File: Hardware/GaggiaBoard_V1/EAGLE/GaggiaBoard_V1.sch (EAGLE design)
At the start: 112 parts, among them IC1 LD117ADT33TR, J10 PIN262409-1, J11 PIN262409-1, J12 PIN262409-1, J13 PIN262409-1, J14 PIN262409-1, J15 PIN262409-1, J16 PIN262409-1, J17 PIN262409-1, J18 PIN262409-1, J19 PIN262409-1, J2 QWIIC_RIGHT_ANGLE, J20 PIN262409-1, J21 PIN262409-1, J22 PIN262409-1, J23 PIN262409-1, J24 5033981892, J3 QWIIC_RIGHT_ANGLE, J4 1X2-3.5MM, J5 1X2-3.5MM, K1 RELAY-SPDT-JZC-11F, K2 RELAY-SPDT-JZC-11F, K3 RELAY-SPDT-JZC-11F, Q1 600mA/40V, Q2 600mA/40V, Q3 600mA/40V, Q4 600mA/40V, Q5 600mA/40V, Q6 600mA/40V, Q8 600mA/40V, Q9 600mA/40V, U1 BLACKPILL, U2 MAX31855K, U3 MAX31855K, U5 TXS0102, U6 TXU0102

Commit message: Layout update
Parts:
- added C12: 1nF/250V, rcl:C-USC0603
- added C13: 10uF/16V, rcl:C-USC0603
- added D5: 1N4007, diode:DIODE-DO214AC
- added IC2: LD117AS33TR, v-reg:LD117AS33TR
- added Q10: 600mA/40V, SparkFun-DiscreteSemi:TRANS_NPN-MMBT2222AL
- added R27, R28: 10K, rcl:R-US_R0603
- IC1: value LD117ADT33TR -> LD117AS33TR; device v-reg:LD117ADT33TR -> v-reg:LD117AS33TR
- J1: LCSC C163037 -> C144395
- J2, J3: value QWIIC_RIGHT_ANGLE -> Vertical Qwiic Connector; device SparkFun-Connectors:QWIIC_CONNECTORJS-1MM -> SparkFun-Connectors:QWIIC_CONNECTOR; LCSC C160404 -> C160390
- J6, J7, J9: device SparkFun-Connectors:CONN_03JST-PTH -> SparkFun-Connectors:CONN_03JST-PTH-VERT; LCSC C157929 -> C131339
- J8: device SparkFun-Connectors:CONN_05JST -> SparkFun-Connectors:CONN_05JST-VERT; LCSC C157923 -> C157993
- R1: value 220K -> 470; device rcl:R-US_R1206 -> rcl:R-US_R0603; LCSC C130275 -> C114669
- R12: value 120 -> 51; LCSC C114640 -> C114628
- R13: value 10K -> 220; device rcl:R-US_R0603 -> rcl:R-US_R2512; LCSC C98220 -> C877859
- R14: value 51 -> 10K; LCSC C114628 -> C98220
- R15: value 220 -> 1K; device rcl:R-US_R2512 -> rcl:R-US_R0603; LCSC C877859 -> C22548
- R20, R21: value 10K -> 220K; device rcl:R-US_R0603 -> rcl:R-US_R1206; LCSC C98220 -> C130275
- R22: value 100 -> 22K; LCSC C105588 -> C114065
- R9: value 470 -> 120; LCSC C114669 -> C114640
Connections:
- new net N$43: C6.2, D5.A, Q10.E
- new net N$44: OK1.A, R15.2
- new net N$45: B1.+, C6.1, R15.1, R22.2
- net 3V3: now also C13.1, IC2.OUT, R14.2, R27.2; no longer R13.2, R21.2
- net 5V: now also IC2.IN, R9.2; no longer R12.2
- net AC_N: now also R21.1; no longer B1.AC2
- net AC_P: now also R20.1; no longer R1.1
- net GND: now also C13.2, IC2.ADJ, R12.1; no longer C6.2, R14.1
- net N$2: now also B1.-, D5.C, Q10.B, R22.1; no longer B1.+, OK1.A
- net N$24: now also R9.1; no longer R10.1
- net N$27: now also R12.2; no longer R14.2
- net N$28: now also R10.1; no longer R11.1
- net N$29: now also R11.1; no longer R12.1
- net N$32: now also R13.2; no longer R15.2
- net N$34: now also R28.2; no longer R20.2
- net N$35: now also R27.1; no longer R21.1
- net N$36: now also B1.AC1, C12.2, R21.2; no longer OK1.COL, R13.1, R22.1
- net N$37: now also B1.AC2, C12.1, R20.2; no longer B1.AC1, R1.2
- net N$39: now also R1.2; no longer R9.2
- net N$7: now also Q10.C; no longer B1.-
- net PA0: now also OK1.COL, R14.1; no longer C6.1, R22.2
- net PB5: now also R28.1; no longer R20.1
- net PB8: now also R1.1; no longer R9.1
- net PUMP_N: now also R13.1; no longer R15.1
- net UART6_5V_RX: now also J1.2; no longer J1.3
- net UART6_5V_TX: now also J1.3; no longer J1.2
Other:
- moved on the sheet: B1, C2, C6, C7, C8, C9, F1, IC1, J22, J23, J9, LED4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

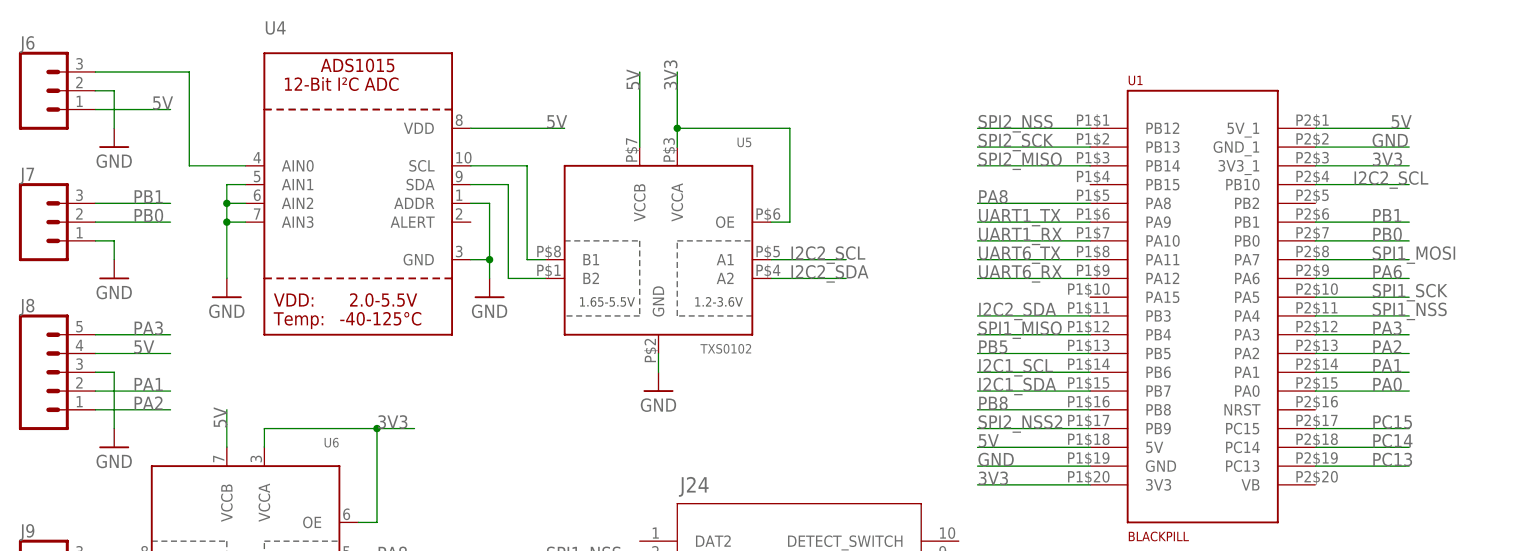
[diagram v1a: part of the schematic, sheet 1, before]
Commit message: Scales port change to PB
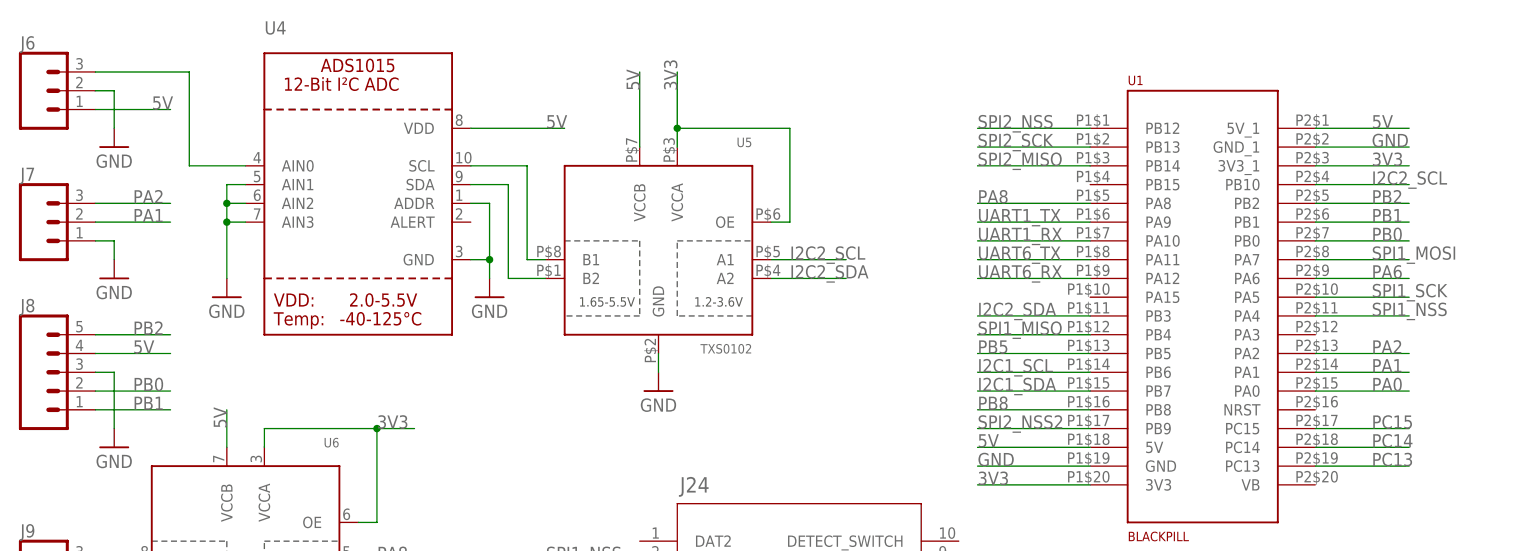
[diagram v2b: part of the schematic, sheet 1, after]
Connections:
- removed net PA3: J8.5, U1.PA3
- new net PB2: J8.5, U1.PB2
- net PA1: now also J7.2; no longer J8.2
- net PA2: now also J7.3; no longer J8.1
- net PB0: now also J8.2; no longer J7.2
- net PB1: now also J8.1; no longer J7.3
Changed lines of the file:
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@@
 <pinref part="U1" gate="G$1" pin="5V_1"/>
 <wire x1="218.44" y1="167.64" x2="231.14" y2="167.64" width="0.1524" layer="91"/>
-<label x="228.6" y="167.64" size="1.778" layer="95"/>
+<label x="226.06" y="167.64" size="1.778" layer="95"/>
 </segment>
 <segment>
@@
 <pinref part="U1" gate="G$1" pin="PB10"/>
 <wire x1="218.44" y1="160.02" x2="231.14" y2="160.02" width="0.1524" layer="91"/>
-<label x="223.52" y="160.02" size="1.778" layer="95"/>
+<label x="226.06" y="160.02" size="1.778" layer="95"/>
 </segment>
 <segment>
@@
 </segment>
 <segment>
-<label x="58.42" y="132.08" size="1.778" layer="95"/>
-<pinref part="J8" gate="G$1" pin="2"/>
-<wire x1="53.34" y1="132.08" x2="63.5" y2="132.08" width="0.1524" layer="91"/>
+<pinref part="J7" gate="J$1" pin="2"/>
+<wire x1="53.34" y1="154.94" x2="63.5" y2="154.94" width="0.1524" layer="91"/>
+<label x="58.42" y="154.94" size="1.778" layer="95"/>
 </segment>
 </net>
@@
 </segment>
 </net>
-<net name="PA3" class="0">
-<segment>
-<pinref part="U1" gate="G$1" pin="PA3"/>
-<wire x1="218.44" y1="139.7" x2="231.14" y2="139.7" width="0.1524" layer="91"/>
-<label x="226.06" y="139.7" size="1.778" layer="95"/>
-</segment>
-<segment>
-<pinref part="J8" gate="G$1" pin="5"/>
-<wire x1="53.34" y1="139.7" x2="63.5" y2="139.7" width="0.1524" layer="91"/>
-<label x="58.42" y="139.7" size="1.778" layer="95"/>
-</segment>
-</net>
 <net name="PA2" class="0">
 <segment>
@@
 </segment>
 <segment>
+<pinref part="J7" gate="J$1" pin="3"/>
+<wire x1="53.34" y1="157.48" x2="63.5" y2="157.48" width="0.1524" layer="91"/>
+<label x="58.42" y="157.48" size="1.778" layer="95"/>
+</segment>
+</net>
+<net name="PB8" class="0">
+<segment>
+<pinref part="U1" gate="G$1" pin="PB8"/>
+<wire x1="187.96" y1="129.54" x2="172.72" y2="129.54" width="0.1524" layer="91"/>
+<label x="172.72" y="129.54" size="1.778" layer="95"/>
+</segment>
+</net>
+<net name="PC15" class="0">
+<segment>
+<pinref part="U1" gate="G$1" pin="PC15"/>
+<wire x1="218.44" y1="127" x2="231.14" y2="127" width="0.1524" layer="91"/>
+<label x="226.06" y="127" size="1.778" layer="95"/>
+</segment>
+</net>
+<net name="PC14" class="0">
+<segment>
+<pinref part="U1" gate="G$1" pin="PC14"/>
+<wire x1="218.44" y1="124.46" x2="231.14" y2="124.46" width="0.1524" layer="91"/>
+<label x="226.06" y="124.46" size="1.778" layer="95"/>
+</segment>
+</net>
+<net name="PC13" class="0">
+<segment>
+<pinref part="U1" gate="G$1" pin="PC13"/>
+<wire x1="218.44" y1="121.92" x2="231.14" y2="121.92" width="0.1524" layer="91"/>
+<label x="226.06" y="121.92" size="1.778" layer="95"/>
+</segment>
+</net>
+<net name="PB0" class="0">
+<segment>
+<pinref part="U1" gate="G$1" pin="PB0"/>
+<wire x1="218.44" y1="152.4" x2="231.14" y2="152.4" width="0.1524" layer="91"/>
+<label x="226.06" y="152.4" size="1.778" layer="95"/>
+</segment>
+<segment>
+<pinref part="J8" gate="G$1" pin="2"/>
+<wire x1="53.34" y1="132.08" x2="63.5" y2="132.08" width="0.1524" layer="91"/>
+<label x="58.42" y="132.08" size="1.778" layer="95"/>
+</segment>
+</net>
+<net name="PB1" class="0">
+<segment>
+<pinref part="U1" gate="G$1" pin="PB1"/>
+<wire x1="218.44" y1="154.94" x2="231.14" y2="154.94" width="0.1524" layer="91"/>
+<label x="226.06" y="154.94" size="1.778" layer="95"/>
+</segment>
+<segment>
 <pinref part="J8" gate="G$1" pin="1"/>
 <wire x1="53.34" y1="129.54" x2="63.5" y2="129.54" width="0.1524" layer="91"/>
 <label x="58.42" y="129.54" size="1.778" layer="95"/>
-</segment>
-</net>
-<net name="PB8" class="0">
-<segment>
-<pinref part="U1" gate="G$1" pin="PB8"/>
-<wire x1="187.96" y1="129.54" x2="172.72" y2="129.54" width="0.1524" layer="91"/>
-<label x="172.72" y="129.54" size="1.778" layer="95"/>
-</segment>
-</net>
-<net name="PC15" class="0">
-<segment>
-<pinref part="U1" gate="G$1" pin="PC15"/>
-<wire x1="218.44" y1="127" x2="231.14" y2="127" width="0.1524" layer="91"/>
-<label x="226.06" y="127" size="1.778" layer="95"/>
-</segment>
-</net>
-<net name="PC14" class="0">
-<segment>
-<pinref part="U1" gate="G$1" pin="PC14"/>
-<wire x1="218.44" y1="124.46" x2="231.14" y2="124.46" width="0.1524" layer="91"/>
-<label x="226.06" y="124.46" size="1.778" layer="95"/>
-</segment>
-</net>
-<net name="PC13" class="0">
-<segment>
-<pinref part="U1" gate="G$1" pin="PC13"/>
-<wire x1="218.44" y1="121.92" x2="231.14" y2="121.92" width="0.1524" layer="91"/>
-<label x="226.06" y="121.92" size="1.778" layer="95"/>
-</segment>
-</net>
-<net name="PB0" class="0">
-<segment>
-<pinref part="U1" gate="G$1" pin="PB0"/>
-<wire x1="218.44" y1="152.4" x2="231.14" y2="152.4" width="0.1524" layer="91"/>
-<label x="226.06" y="152.4" size="1.778" layer="95"/>
-</segment>
-<segment>
-<pinref part="J7" gate="J$1" pin="2"/>
-<wire x1="53.34" y1="154.94" x2="63.5" y2="154.94" width="0.1524" layer="91"/>
-<label x="58.42" y="154.94" size="1.778" layer="95"/>
-</segment>
-</net>
-<net name="PB1" class="0">
-<segment>
-<pinref part="U1" gate="G$1" pin="PB1"/>
-<wire x1="218.44" y1="154.94" x2="231.14" y2="154.94" width="0.1524" layer="91"/>
-<label x="226.06" y="154.94" size="1.778" layer="95"/>
-</segment>
-<segment>
-<pinref part="J7" gate="J$1" pin="3"/>
-<wire x1="53.34" y1="157.48" x2="63.5" y2="157.48" width="0.1524" layer="91"/>
-<label x="58.42" y="157.48" size="1.778" layer="95"/>
 </segment>
 </net>
@@
 </segment>
 </net>
+<net name="PB2" class="0">
+<segment>
+<pinref part="U1" gate="G$1" pin="PB2"/>
+<wire x1="218.44" y1="157.48" x2="231.14" y2="157.48" width="0.1524" layer="91"/>
+<label x="226.06" y="157.48" size="1.778" layer="95"/>
+</segment>
+<segment>
+<pinref part="J8" gate="G$1" pin="5"/>
+<wire x1="53.34" y1="139.7" x2="63.5" y2="139.7" width="0.1524" layer="91"/>
+<label x="58.42" y="139.7" size="1.778" layer="95"/>
+</segment>
+</net>

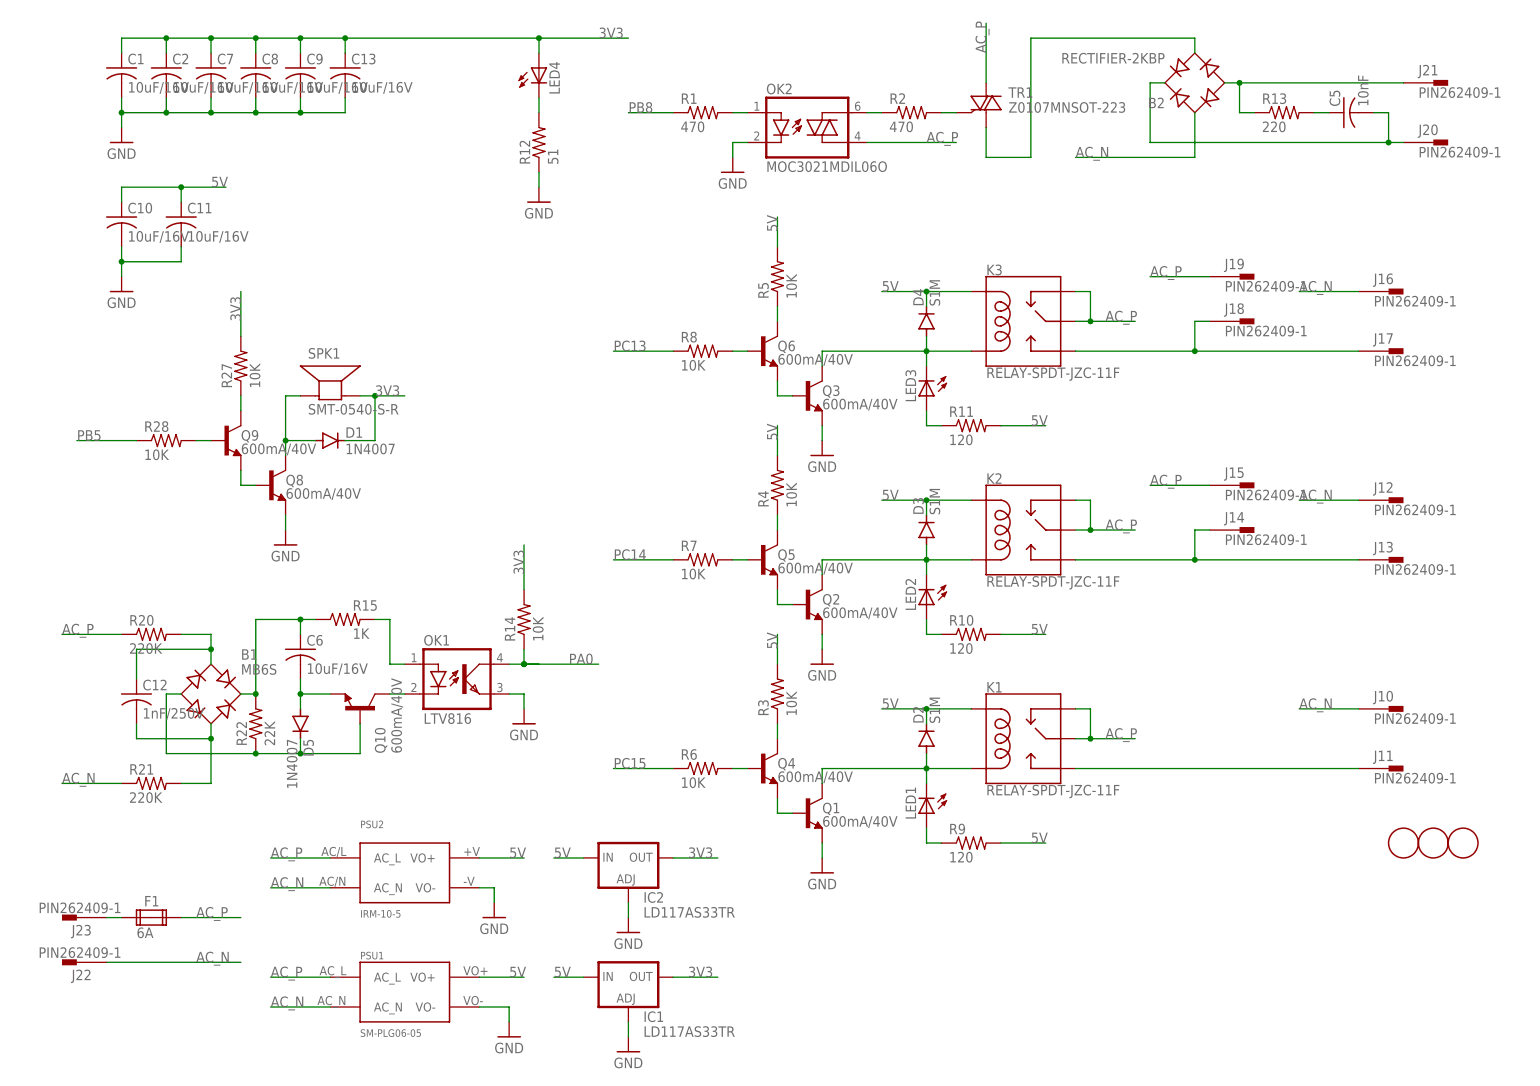
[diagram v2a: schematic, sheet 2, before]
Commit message: Pump bridge rectifier removed, SSR control changed
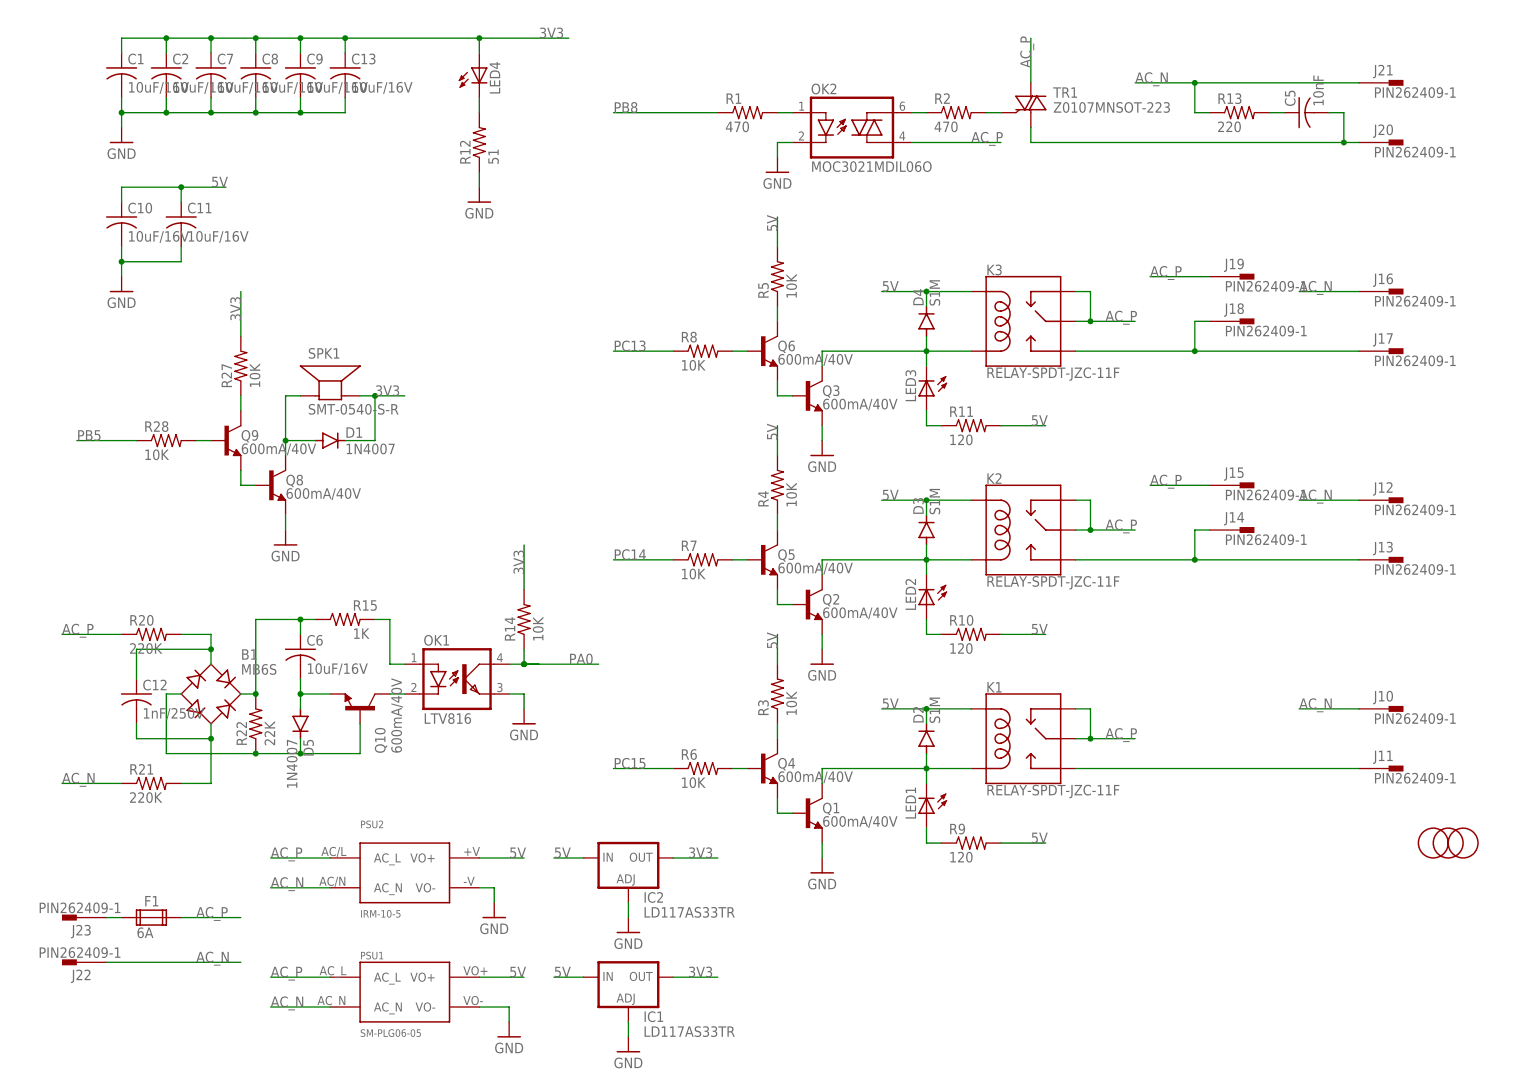
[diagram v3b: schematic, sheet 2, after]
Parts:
- removed B2: RECTIFIER-2KBP, rectifier:RECTIFIER-2KBP
- removed U6: TXU0102, microbuilder:TXS0102
- added C14: 0.1uF, rcl:C-USC0603
- added D6: (no value), adafruit:DIODESOD-123
- added Q11: MOSFET_PCH_DUAL-DMP2240UDM, SparkFun-DiscreteSemi:MOSFET_PCH_DUAL-DMP2240UDM
- added Q12: (no value), SparkFun-DiscreteSemi:TRANS_NPN_DUAL-MBT3904DW1T1
- added R29, R33, R34: 10K, rcl:R-US_R0603
- added R30: 1K, rcl:R-US_R0603
- added R31, R32: 120K, rcl:R-US_R0603
- J27: device SparkFun-Connectors:CONN_041X04_NO_SILK -> SparkFun-Connectors:CONN_05NO_SILK
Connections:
- removed net N$40: B2.AC2, TR1.A1
- removed net PUMP_N: B2.-, J21.1, R13.1
- new net N$46: Q12Q2.B, R33.1
- new net N$47: Q11G$1.G, Q12Q1.C, R32.1
- new net N$48: Q11G1.G, Q12Q2.C, R31.1
- new net N$49: Q12Q1.B, R34.1
- new net NRST: C14.2, D6.A, R29.1, U1.NRST
- new net RTS: C14.1, J27.5, R30.2
- net 3V3: now also D6.C, R29.2; no longer U6.OE, U6.VCCA
- net 5V: now also Q11G$1.S, Q11G1.S, R31.2, R32.2; no longer U6.VCCB
- net AC_N: now also J21.1, R13.1; no longer B2.AC1
- net GND: now also Q12Q1.E, Q12Q2.E, R30.1; no longer U6.GND
- net N$41: now also J9.2, Q11G$1.D; no longer J9.3, U6.B1
- net N$42: now also J9.3, Q11G1.D; no longer J9.2, U6.B2
- net PA6: now also R34.2; no longer U6.A2
- net PA8: now also R33.2; no longer U6.A1
- net PUMP_P: now also TR1.A1; no longer B2.+
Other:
- moved on the sheet: C5, J20, J21, J9, LED4, OK2, R1, R12, R13, R2, TR1
